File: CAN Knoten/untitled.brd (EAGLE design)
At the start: 160 x 100 mm, 39 parts, among them Q1 HC49-U - 16MHz, Q2 HC49-U - xMHz

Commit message: 
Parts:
- moved J1 190.8 mm to (44.6, 35.8)
- moved D1 149.5 mm to (27.0, 40.2)
- moved C2 23.7 mm to (33.5, 4.40)
- moved C3 23.7 mm to (28.4, 4.40)
- moved Q1 23.7 mm to (30.9, 8.21)
- moved U$1 23.7 mm to (30.9, 17.1)
- moved U$2 23.7 mm to (30.9, 27.3)
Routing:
- net N$13: track 0.00 -> 224.0 mm
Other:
- board outline removed

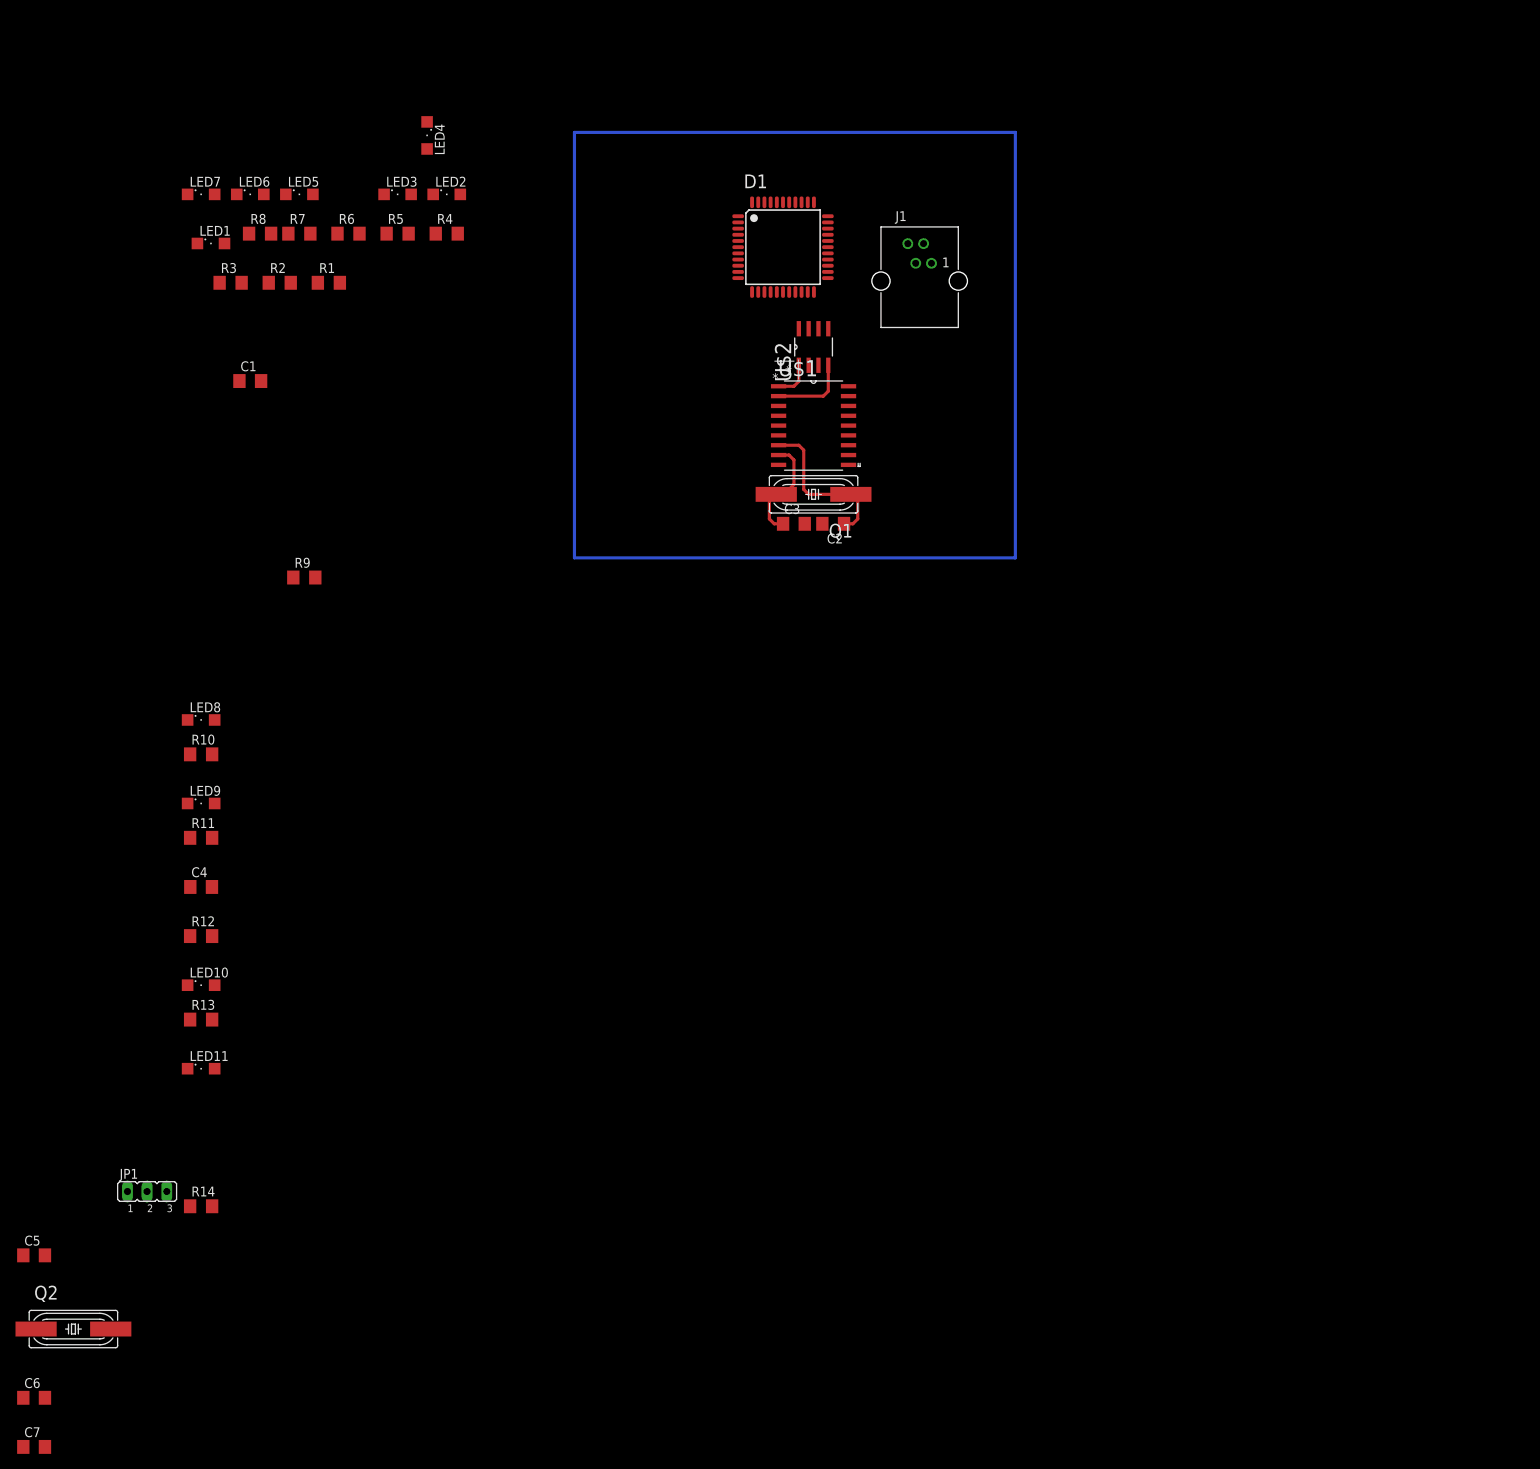
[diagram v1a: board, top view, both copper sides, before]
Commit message: 
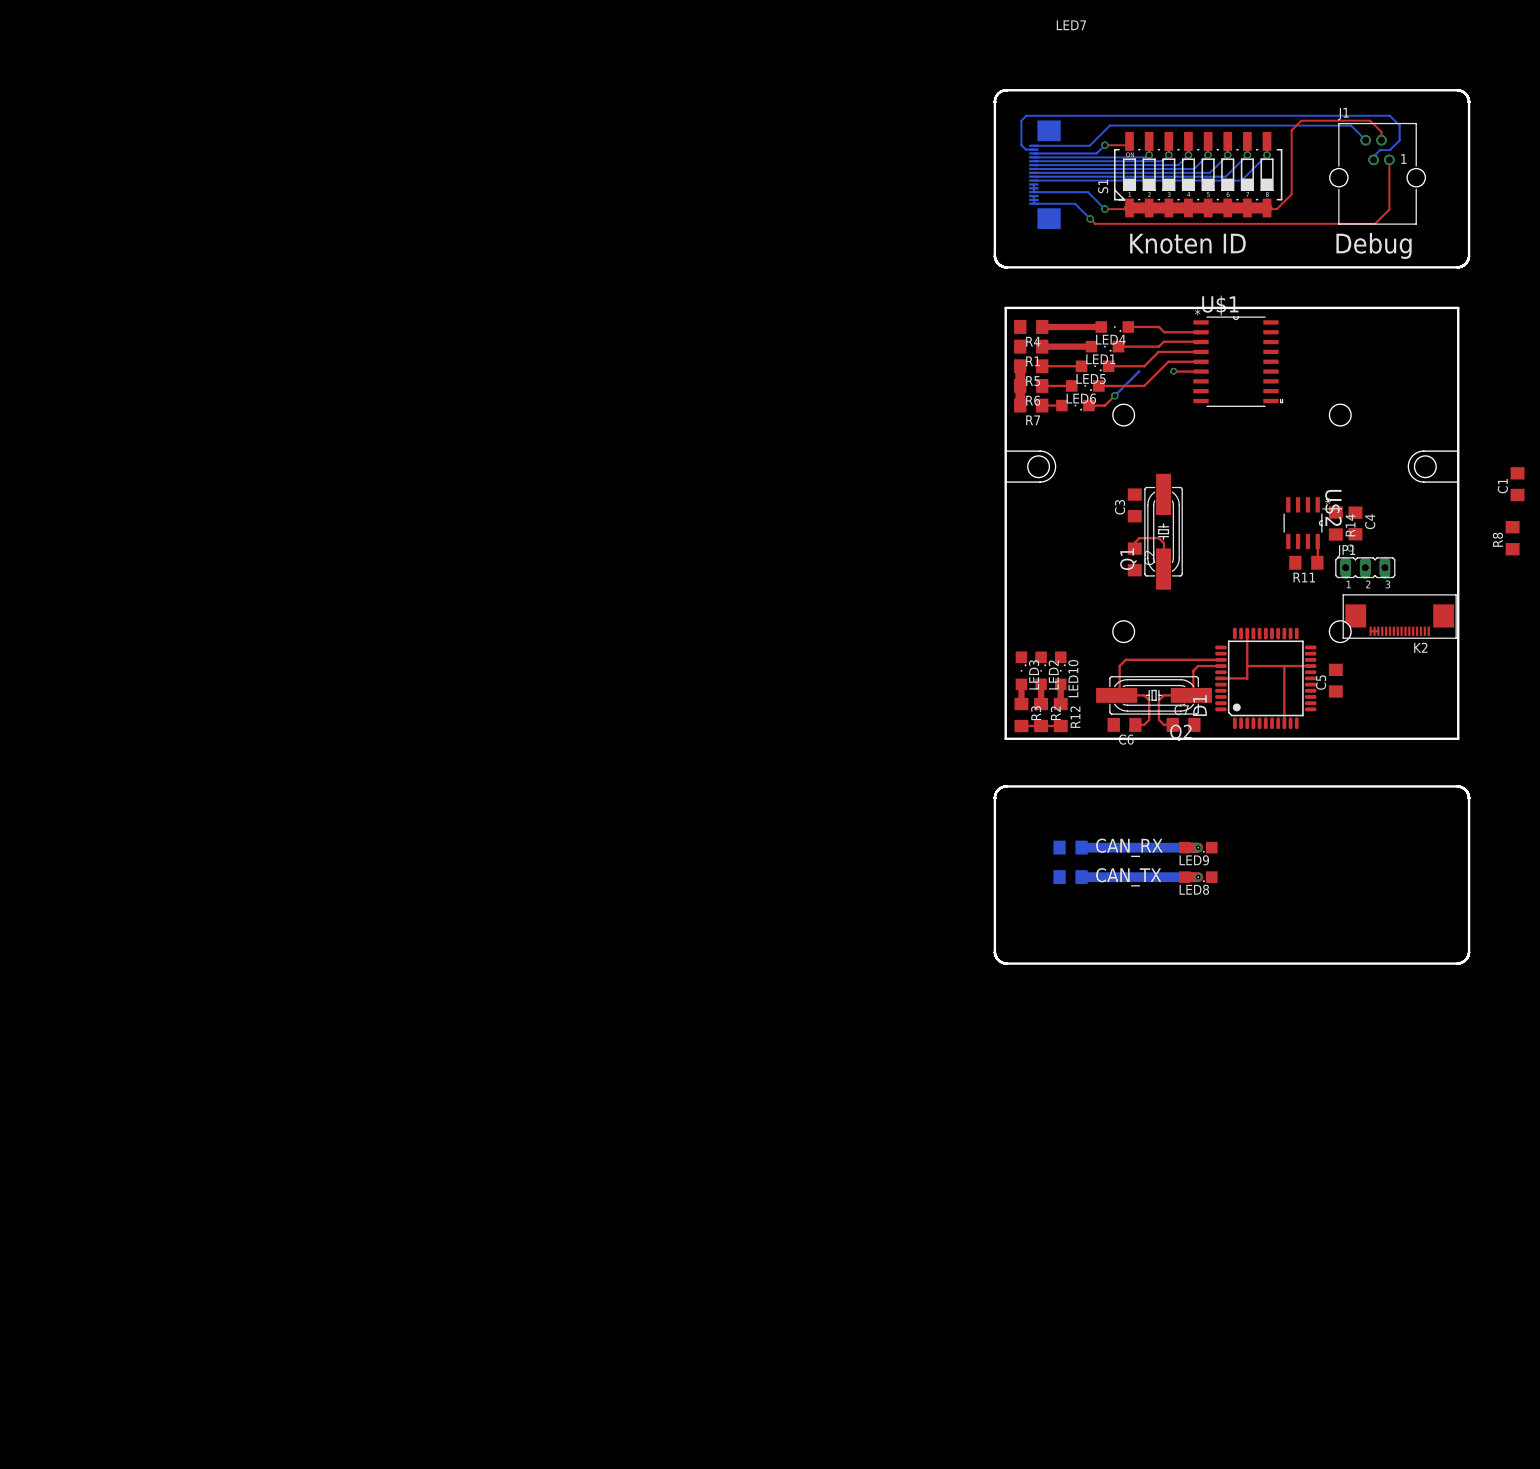
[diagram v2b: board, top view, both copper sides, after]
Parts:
- removed LED11: (no value), led:SML1206
- removed R13: 560R, rcl:R1206
- added K1, K2: 68711614522, Wurth_FPC_FFC:68711614522
- added S1: 219-08, switch-dil:CTS-219-08
- added U$3: (no value), RND 455-00879:RND_455-00879_X4
- moved C5 183.9 mm to (98.4, -15.9), turned to 90 degrees
- moved JP1 176.9 mm to (102.2, -1.27)
- moved C7 175.5 mm to (78.7, -21.6)
- moved R14 171.2 mm to (98.4, 4.45), turned to 270 degrees
- moved R8 166.6 mm to (121.3, 2.54), turned to 90 degrees
- moved C6 165.7 mm to (71.1, -21.6), turned to 180 degrees
- moved C1 164.4 mm to (121.9, 9.53), turned to 90 degrees
- moved Q2 161.9 mm to (74.9, -17.8), turned to 180 degrees
- moved C4 156.4 mm to (101.0, 4.45), turned to 270 degrees
- moved R11 147.2 mm to (94.6, -0.64), turned to 180 degrees
- moved LED8 130.5 mm to (80.6, -41.3), turned to 180 degrees
- moved LED9 129.0 mm to (80.6, -37.5), turned to 180 degrees
- moved LED10 118.3 mm to (62.9, -14.6), turned to 270 degrees
- moved R3 116.5 mm to (57.8, -20.3), turned to 270 degrees
- moved LED1 116.3 mm to (68.6, 27.3), turned to 180 degrees
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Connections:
- removed net N$10: LED11.A, R13.1
- new net FRONT_DEBUG_RXD: J1.4, K1.1
- new net FRONT_DEBUG_TXD: J1.3, K1.2
- new net FRONT_GND: J1.2, K1.11, K1.12, K1.13, S1.1, S1.2, S1.3, S1.4, S1.5, S1.6, S1.7, S1.8
- new net FRONT_VCC: J1.1, K1.14, K1.15, K1.16
- new net N$22: K1.3, S1.16
- new net N$23: K1.4, S1.15
- new net N$24: K1.5, S1.14
- new net N$25: K1.6, S1.13
- new net N$26: K1.7, S1.12
- new net N$27: K1.8, S1.11
- new net N$28: K1.9, S1.10
- new net N$29: K1.10, S1.9
- new net N$33: K2.3
- new net N$34: K2.4
- new net N$35: K2.5
- new net N$36: K2.6
- new net N$37: K2.7
- new net N$38: K2.8
- new net N$39: K2.9
- new net N$40: K2.10
- net DEBUG_RXD: now also K2.1; no longer J1.4
- net DEBUG_TXD: now also K2.2; no longer J1.3
- net GND: now also K2.11, K2.12, K2.13; no longer J1.2
- net MCP2515_OSC2: no longer LED11.C
- net VCC: now also K2.14, K2.15, K2.16; no longer J1.1, R13.2
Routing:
- net N$13: track 224.0 -> 0.00 mm
- net FRONT_DEBUG_TXD: track 0.00 -> 61.3 mm
- net FRONT_GND: track 0.00 -> 58.2 mm, vias 0 -> 1
- net FRONT_VCC: track 0.00 -> 55.2 mm, vias 0 -> 1
- net FRONT_DEBUG_RXD: track 0.00 -> 44.8 mm
- net VCC: track 0.00 -> 36.0 mm, vias 0 -> 1
- net N$29: track 0.00 -> 33.3 mm, vias 0 -> 1
- net N$28: track 0.00 -> 30.5 mm, vias 0 -> 1
- net N$27: track 0.00 -> 27.8 mm, vias 0 -> 1
- net N$15: track 0.00 -> 26.4 mm
- net N$26: track 0.00 -> 25.0 mm, vias 0 -> 1
- net N$25: track 0.00 -> 22.3 mm, vias 0 -> 1
- net N$24: track 0.00 -> 19.5 mm, vias 0 -> 1
- net N$9: track 0.00 -> 16.8 mm, vias 0 -> 1
- net N$8: track 0.00 -> 16.8 mm, vias 0 -> 1
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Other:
- board outline added: 61.3 x 112.9 mm
- board text added: "CAN_RX"
- board text added: "CAN_TX"
- board text added: "Debug"
- board text added: "Knoten ID"

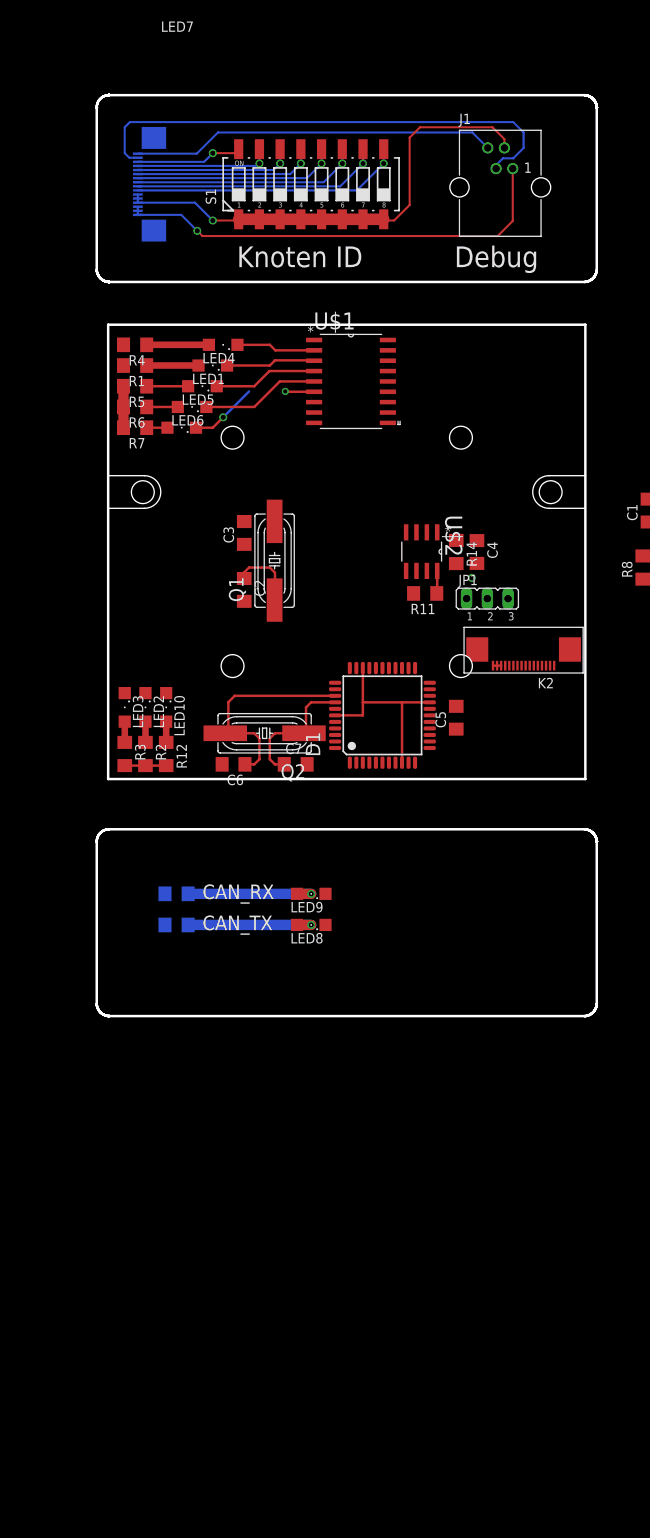
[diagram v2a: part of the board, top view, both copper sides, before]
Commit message: 
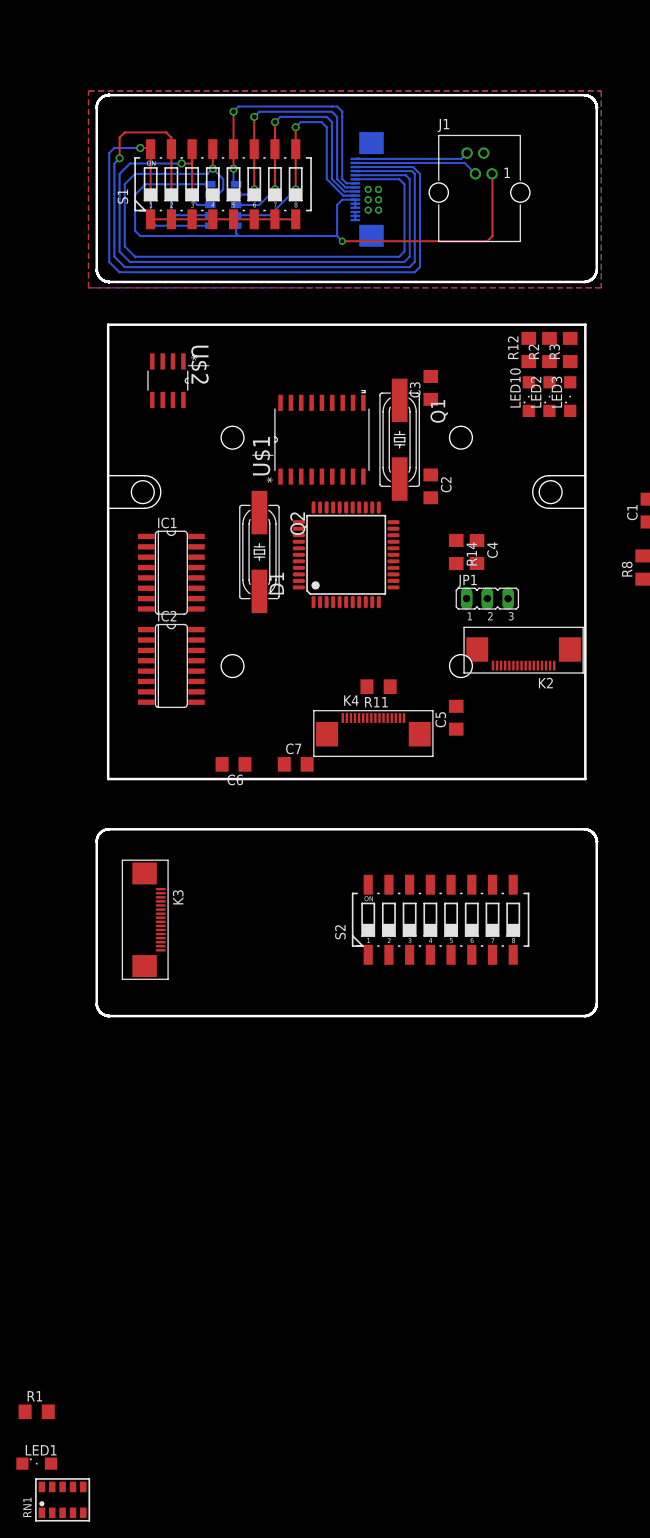
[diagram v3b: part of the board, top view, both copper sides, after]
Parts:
- removed LED4, LED5, LED6, LED7, LED8, LED9: (no value), led:SML1206
- removed R10, R4, R5, R6, R7, R9: 560R, rcl:R1206
- added IC1, IC2: 74LS165D, 74xx-us:SO16
- added K3, K4: 68711614522, Wurth_FPC_FFC:68711614522
- added RN1, RN3: (no value), resistor-array:745-10
- added S2: 219-08, switch-dil:CTS-219-08
- moved LED1 136.3 mm to (47.0, -107.3), turned to 0 degrees
- moved R1 128.8 mm to (47.0, -101.0), turned to 0 degrees
- moved R3 73.7 mm to (112.4, 29.2), turned to 90 degrees
- moved R2 70.0 mm to (109.9, 29.2), turned to 90 degrees
- moved LED3 66.6 mm to (112.4, 23.5), turned to 90 degrees
- moved R12 66.6 mm to (107.3, 29.2), turned to 90 degrees
- moved LED2 62.5 mm to (109.9, 23.5), turned to 90 degrees
- moved LED10 58.5 mm to (107.3, 23.5), turned to 90 degrees
- moved U$2 37.5 mm to (63.1, 25.4)
- moved C3 29.0 mm to (95.3, 24.6)
- moved K1 26.7 mm to (86.7, 48.9)
- moved C2 26.2 mm to (95.3, 12.5)
- moved Q2 22.2 mm to (74.3, 4.45), turned to 270 degrees
- moved Q1 21.3 mm to (91.5, 18.2), turned to 270 degrees
- moved D1 20.2 mm to (84.9, 4.10)
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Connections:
- removed net N$33: K2.3
- removed net N$34: K2.4
- removed net N$35: K2.5
- removed net N$36: K2.6
- removed net N$37: K2.7
- removed net N$38: K2.8
- removed net N$39: K2.9
- removed net N$40: K2.10
- new net 74XX165_CLK: D1.4, IC1.2, IC2.2
- new net 74XX165_OUT: D1.7, IC2.9
- new net 74XX165_SH/LD_IC1: D1.5, IC1.1
- new net 74XX165_SH/LD_IC2: D1.6, IC2.1
- new net CAN_BITRATE_0: IC2.11, K4.3
- new net CAN_BITRATE_1: IC2.12, K4.4
- new net CAN_BITRATE_2: IC2.13, K4.5
- new net CAN_BITRATE_3: IC2.14, K4.6
- new net CAN_BITRATE_4: IC2.3, K4.7
- new net CAN_BITRATE_5: IC2.4, K4.8
- new net CAN_BITRATE_6: IC2.5, K4.9
- new net CAN_BITRATE_7: IC2.6, K4.10
- new net N$13: D1.40
- new net N$14: D1.41
- new net N$18: D1.42
- new net N$19: K3.9, RN1.8, S2.10
- new net N$2: IC1.9, IC2.10
- new net N$30: K3.10, RN1.9, S2.9
- new net N$31: D1.21
- new net NODE_ID_0: IC1.11, K2.3
- new net NODE_ID_1: IC1.12, K2.4
- new net NODE_ID_2: IC1.13, K2.5
- new net NODE_ID_3: IC1.14, K2.6
- new net NODE_ID_4: IC1.3, K2.7
- new net NODE_ID_5: IC1.4, K2.8
- new net NODE_ID_6: IC1.5, K2.9
- new net NODE_ID_7: IC1.6, K2.10
- new net REAR_GND: K3.14, K3.15, K3.16, S2.1, S2.2, S2.3, S2.4, S2.5, S2.6, S2.7, S2.8
- new net REAR_VCC: K3.1, K3.11, K3.12, K3.13, K3.2, RN1.10, RN1.5
- net FRONT_GND: now also K1.14, K1.15, K1.16; no longer K1.11, K1.12, K1.13
- net FRONT_VCC: now also K1.11, K1.12, K1.13, RN3.10, RN3.5; no longer K1.14, K1.15, K1.16
- net GND: now also IC1.15, IC1.8, IC2.15, IC2.8, K2.14, K2.15, K2.16, K4.14, K4.15, K4.16; no longer K2.11, K2.12, K2.13
- net MCP2515_CLKOUT: no longer LED1.C
- net MCP2515_INT: now also D1.43
- net MCP2515_RXCAN: now also D1.44; no longer LED4.C, LED9.C
- net MCP2515_TX0RTS: now also D1.1; no longer LED5.C
- net MCP2515_TX1RTS: now also D1.2; no longer LED6.C
- net MCP2515_TX2RTS: now also D1.3; no longer LED7.C
- net MCP2515_TXCAN: no longer LED8.C
- net N$22: now also RN3.1
- net N$23: now also RN3.2
- net N$24: now also RN3.3
- net N$25: now also RN3.4
- net N$26: now also RN3.6
- net N$27: now also RN3.7
- net N$28: now also RN3.8
- net N$29: now also RN3.9
- net N$4: now also K3.3, RN1.1, S2.16; no longer LED4.A, R4.1
- net N$5: now also K3.4, RN1.2, S2.15; no longer LED5.A, R5.1
- net N$6: now also K3.5, RN1.3, S2.14; no longer LED6.A, R6.1
- net N$7: now also K3.6, RN1.4, S2.13; no longer LED7.A, R7.1
- net N$8: now also K3.7, RN1.6, S2.12; no longer LED8.A, R9.1
- net N$9: now also K3.8, RN1.7, S2.11; no longer LED9.A, R10.1
- net SPI_SLAVE_SELECT_HW: now also LED1.C
- net VCC: now also IC1.16, IC2.16, K2.11, K2.12, K2.13, K4.1, K4.11, K4.12, K4.13, K4.2; no longer K2.14, K2.15, K2.16, R10.2, R4.2, R5.2, R6.2, R7.2, R9.2
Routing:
- net N$22: track 13.0 -> 93.6 mm, vias 1 -> 2
- net N$23: track 16.8 -> 91.5 mm, vias 1 -> 2
- net N$24: track 19.5 -> 80.4 mm, vias 1 -> 2
- net N$25: track 22.3 -> 76.1 mm
- net FRONT_DEBUG_TXD: track 61.3 -> 15.3 mm
- net FRONT_GND: track 58.2 -> 18.8 mm, vias 1 -> 6
- net VCC: track 36.0 -> 0.00 mm, vias 1 -> 0
- net FRONT_DEBUG_RXD: track 44.8 -> 14.0 mm
- net N$15: track 26.4 -> 0.00 mm
- net FRONT_VCC: track 55.2 -> 75.2 mm
- net N$9: track 16.8 -> 0.00 mm, vias 1 -> 0
- net N$8: track 16.8 -> 0.00 mm, vias 1 -> 0
- net N$16: track 16.1 -> 0.00 mm
- net MCP2515_TX1RTS: track 14.5 -> 0.00 mm
- net MCP2515_TX0RTS: track 12.7 -> 0.00 mm
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- added copper zone on layer 1, net FRONT_GND
- added copper zone on layer 16, net FRONT_GND
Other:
- board text removed: "CAN_RX"
- board text removed: "CAN_TX"
- board text removed: "Debug"
- board text removed: "Knoten ID"
